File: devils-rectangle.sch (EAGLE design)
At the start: 26 parts, among them J3 CORTEX_DEBUG_PTH, J6 USB-MICROB, U1 ATSAMD21G-M, U2 MIC5501-3.0YM5-TR, U3 TPD2S017, Y1 32.768KHZ

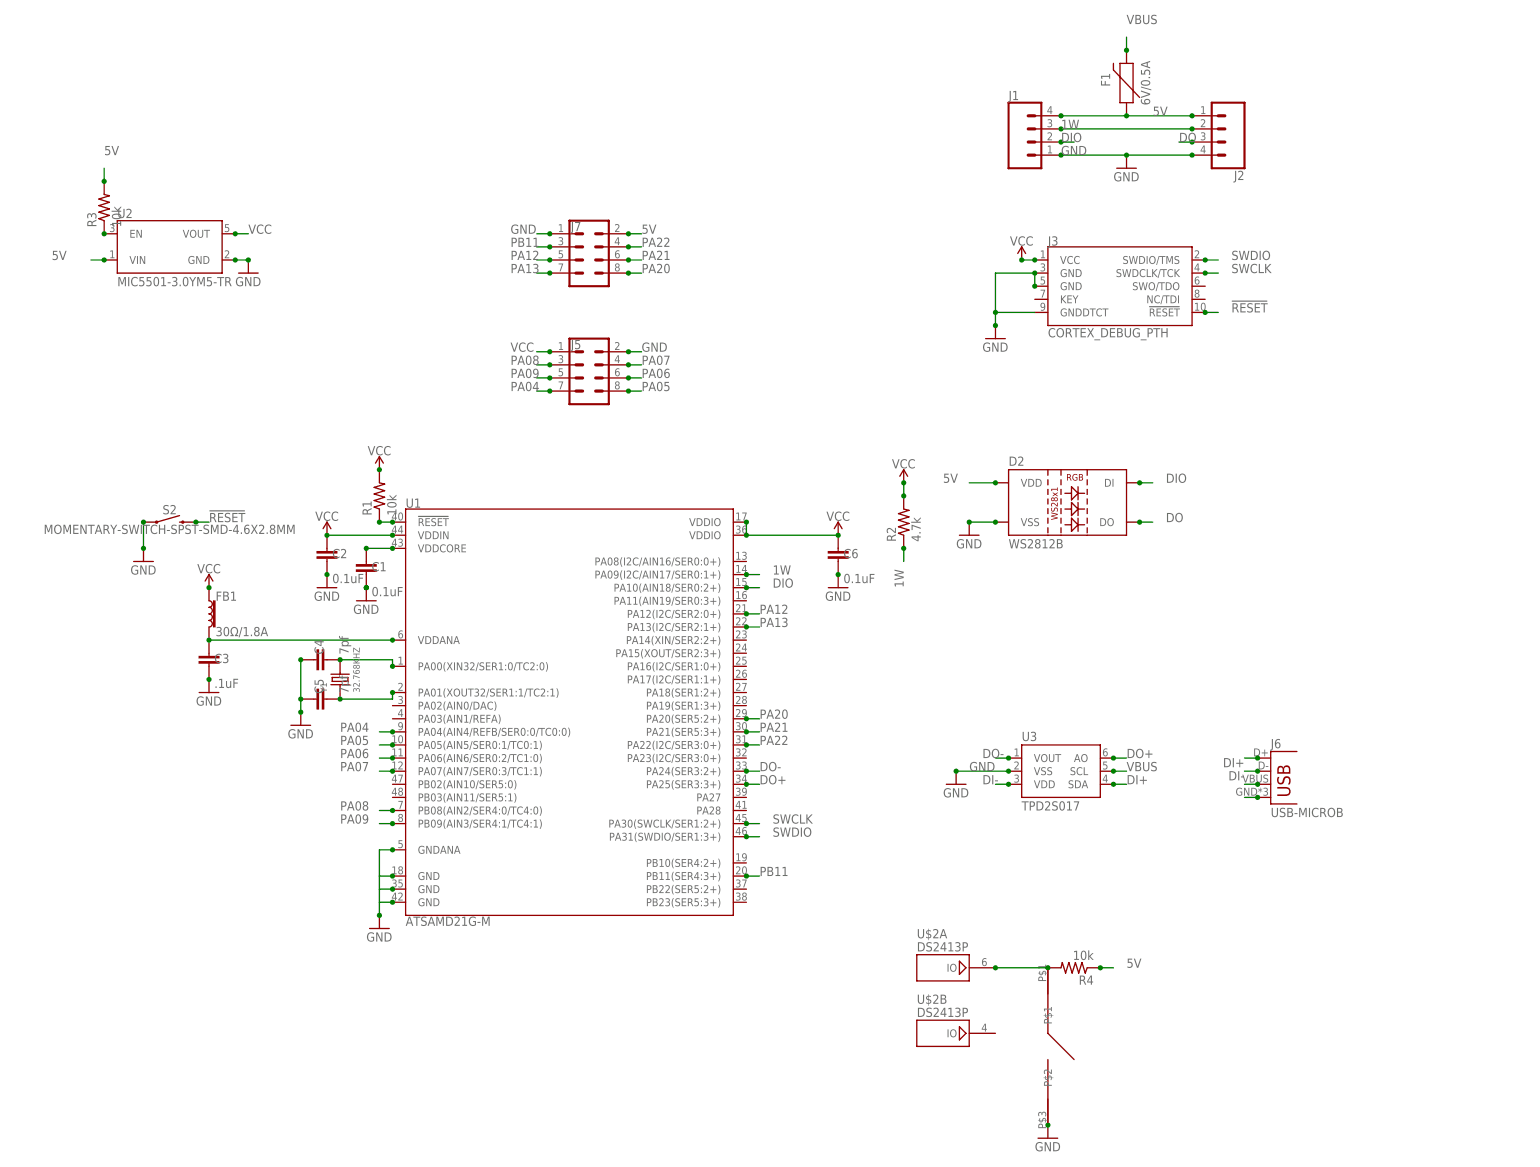
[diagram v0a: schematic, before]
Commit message: resolved routing errors
resolved routing errors, added crystal, and tested. submitted to oshpark.
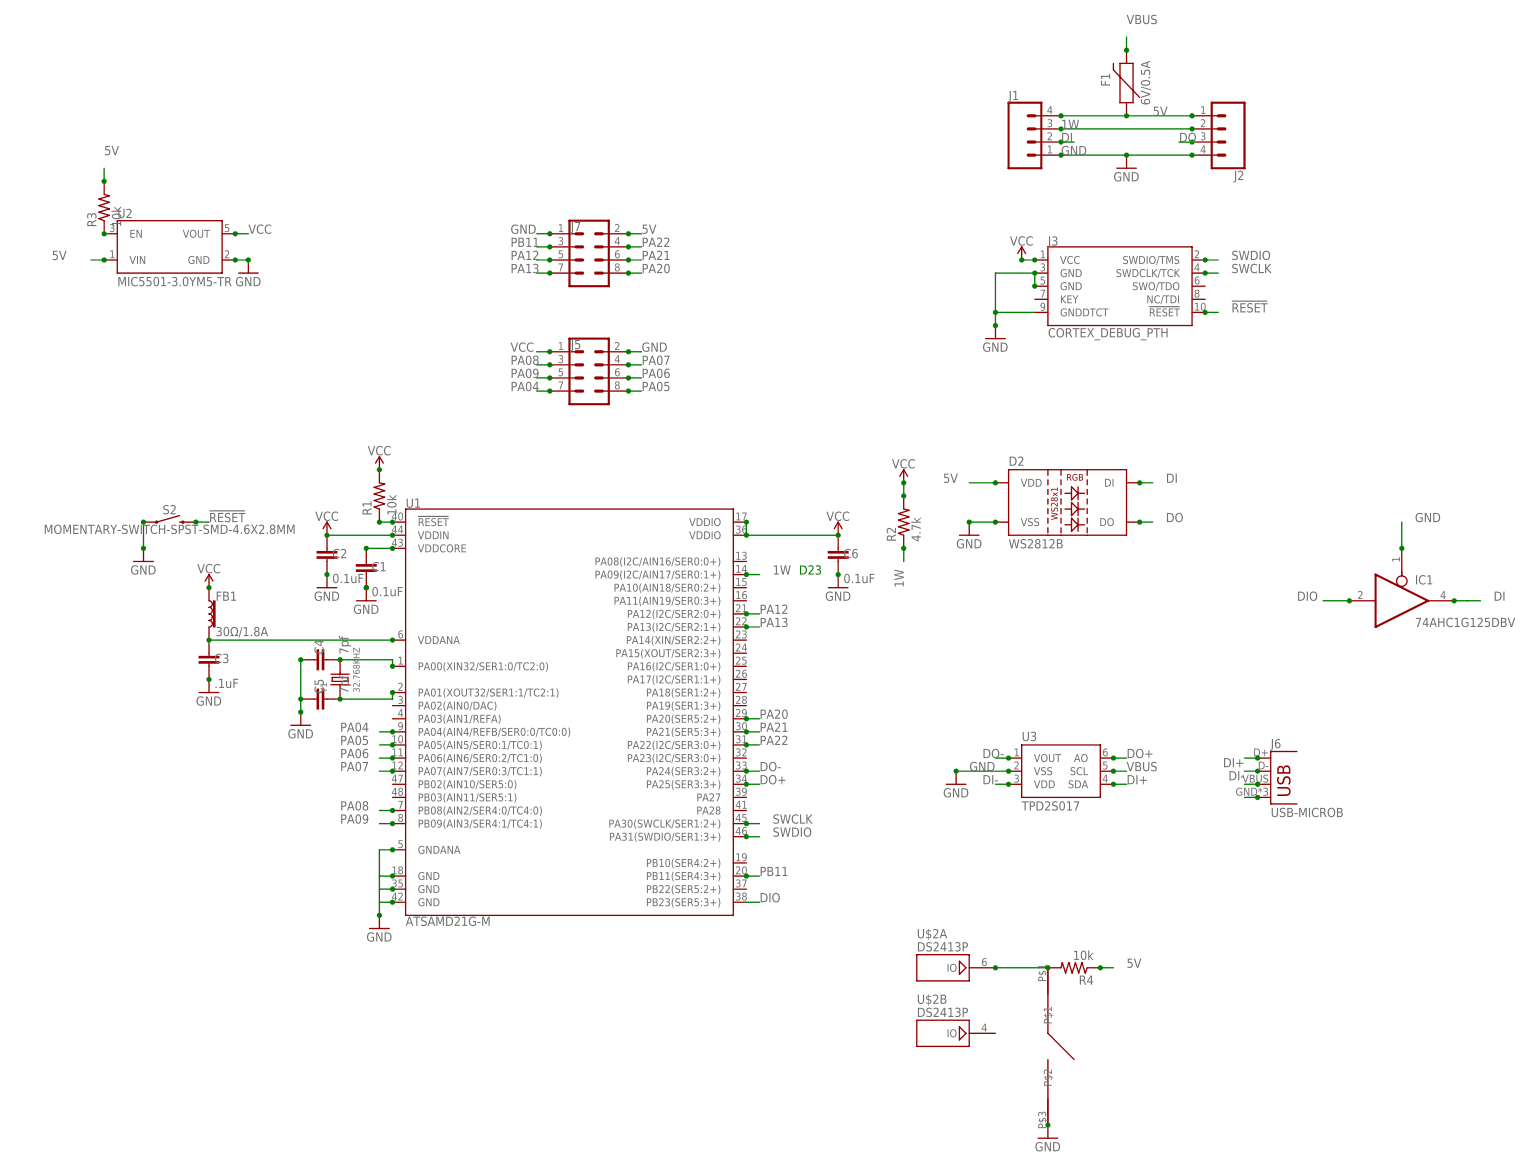
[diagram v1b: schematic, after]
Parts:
- added IC1: 74AHC1G125DBV, 74xx-custom:74AHC1G125DBV
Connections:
- new net DI: D2.DI, IC1A.O, J1.2
- net DIO: now also IC1A.I, U1.PB23(SER5:3+); no longer D2.DI, J1.2, U1.PA10(AIN18/SER0:2+)
- net GND: now also IC1A.OE
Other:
- note added: "D23"
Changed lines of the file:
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@@
 <part name="C5" library="SparkFun-Capacitors" library_urn="urn:adsk.eagle:library:510" deviceset="0.1UF" device="-0402-16V-10%" package3d_urn="urn:adsk.eagle:package:37413/1" value="7pf"/>
 <part name="GND13" library="supply1" library_urn="urn:adsk.eagle:library:371" deviceset="GND" device=""/>
+<part name="IC1" library="74xx-custom" deviceset="74*1G125" device="DBV" package3d_urn="urn:adsk.eagle:package:2482/1" technology="AHC"/>
 </parts>
 <sheets>
 <sheet>
 <plain>
+<text x="238.76" y="137.16" size="1.778" layer="91">D23</text>
 </plain>
 <instances>
@@
 <instance part="GND13" gate="1" x="142.24" y="107.95" smashed="yes">
 <attribute name="VALUE" x="139.7" y="105.41" size="1.778" layer="96"/>
+</instance>
+<instance part="IC1" gate="A" x="355.6" y="132.08" smashed="yes">
+<attribute name="NAME" x="358.14" y="135.255" size="1.778" layer="95"/>
+<attribute name="VALUE" x="358.14" y="127" size="1.778" layer="96"/>
 </instance>
 </instances>
@@
 <junction x="142.24" y="110.49"/>
 </segment>
+<segment>
+<pinref part="IC1" gate="A" pin="OE"/>
+<wire x1="355.6" y1="142.24" x2="355.6" y2="147.32" width="0.1524" layer="91"/>
+<label x="358.14" y="147.32" size="1.778" layer="95"/>
+<junction x="355.6" y="142.24"/>
+</segment>
 </net>
 <net name="N$4" class="0">
@@
 <net name="DIO" class="0">
 <segment>
-<pinref part="U1" gate="G$1" pin="PA10(AIN18/SER0:2+)"/>
-<wire x1="228.6" y1="134.62" x2="231.14" y2="134.62" width="0.1524" layer="91"/>
-<label x="233.68" y="134.62" size="1.778" layer="95"/>
-<junction x="228.6" y="134.62"/>
-</segment>
-<segment>
-<pinref part="J1" gate="G$1" pin="2"/>
-<wire x1="289.56" y1="220.98" x2="292.1" y2="220.98" width="0.1524" layer="91"/>
-<label x="289.56" y="220.98" size="1.778" layer="95"/>
-<junction x="289.56" y="220.98"/>
-</segment>
-<segment>
-<pinref part="D2" gate="G$1" pin="DI"/>
-<wire x1="307.34" y1="154.94" x2="304.8" y2="154.94" width="0.1524" layer="91"/>
-<junction x="304.8" y="154.94"/>
-<label x="309.88" y="154.94" size="1.778" layer="95"/>
+<pinref part="IC1" gate="A" pin="I"/>
+<wire x1="345.44" y1="132.08" x2="340.36" y2="132.08" width="0.1524" layer="91"/>
+<label x="335.28" y="132.08" size="1.778" layer="95"/>
+<junction x="345.44" y="132.08"/>
+</segment>
+<segment>
+<pinref part="U1" gate="G$1" pin="PB23(SER5:3+)"/>
+<wire x1="228.6" y1="73.66" x2="231.14" y2="73.66" width="0.1524" layer="91"/>
+<label x="231.14" y="73.66" size="1.778" layer="95"/>
 </segment>
 </net>
@@
 </segment>
 </net>
+<net name="DI" class="0">
+<segment>
+<pinref part="D2" gate="G$1" pin="DI"/>
+<wire x1="307.34" y1="154.94" x2="304.8" y2="154.94" width="0.1524" layer="91"/>
+<junction x="304.8" y="154.94"/>
+<label x="309.88" y="154.94" size="1.778" layer="95"/>
+</segment>
+<segment>
+<pinref part="IC1" gate="A" pin="O"/>
+<wire x1="365.76" y1="132.08" x2="368.3" y2="132.08" width="0.1524" layer="91"/>
+<wire x1="370.84" y1="132.08" x2="368.3" y2="132.08" width="0.1524" layer="91"/>
+<label x="373.38" y="132.08" size="1.778" layer="95"/>
+<junction x="365.76" y="132.08"/>
+</segment>
+<segment>
+<pinref part="J1" gate="G$1" pin="2"/>
+<wire x1="289.56" y1="220.98" x2="292.1" y2="220.98" width="0.1524" layer="91"/>
+<label x="289.56" y="220.98" size="1.778" layer="95"/>
+<junction x="289.56" y="220.98"/>
+</segment>
+</net>

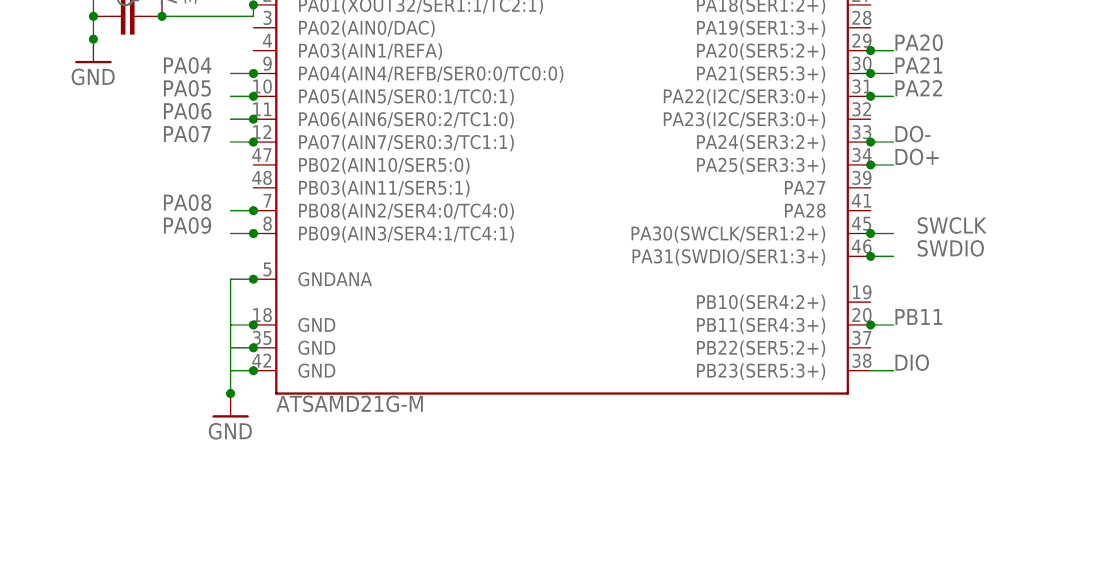
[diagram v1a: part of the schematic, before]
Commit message: sent to fab
sent to fab, errors on board
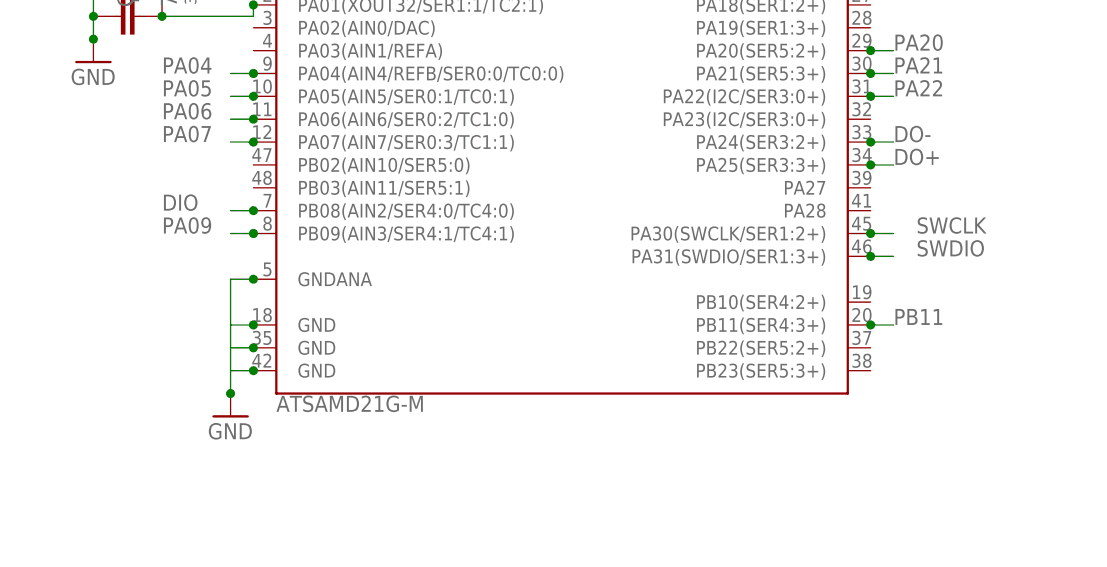
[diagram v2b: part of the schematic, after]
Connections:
- net DIO: now also U1.PB08(AIN2/SER4:0/TC4:0); no longer U1.PB23(SER5:3+)
- net PA08: no longer U1.PB08(AIN2/SER4:0/TC4:0)
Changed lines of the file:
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@@
 </segment>
 <segment>
-<pinref part="U1" gate="G$1" pin="PB23(SER5:3+)"/>
-<wire x1="228.6" y1="73.66" x2="231.14" y2="73.66" width="0.1524" layer="91"/>
-<label x="231.14" y="73.66" size="1.778" layer="95"/>
+<pinref part="U1" gate="G$1" pin="PB08(AIN2/SER4:0/TC4:0)"/>
+<wire x1="160.02" y1="91.44" x2="157.48" y2="91.44" width="0.1524" layer="91"/>
+<junction x="160.02" y="91.44"/>
+<label x="149.86" y="91.44" size="1.778" layer="95"/>
 </segment>
 </net>
@@
 <net name="PA08" class="0">
 <segment>
-<pinref part="U1" gate="G$1" pin="PB08(AIN2/SER4:0/TC4:0)"/>
-<wire x1="160.02" y1="91.44" x2="157.48" y2="91.44" width="0.1524" layer="91"/>
-<junction x="160.02" y="91.44"/>
-<label x="149.86" y="91.44" size="1.778" layer="95"/>
-</segment>
-<segment>
 <pinref part="J5" gate="G$1" pin="3"/>
